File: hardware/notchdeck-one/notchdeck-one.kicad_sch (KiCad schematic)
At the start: 0 parts

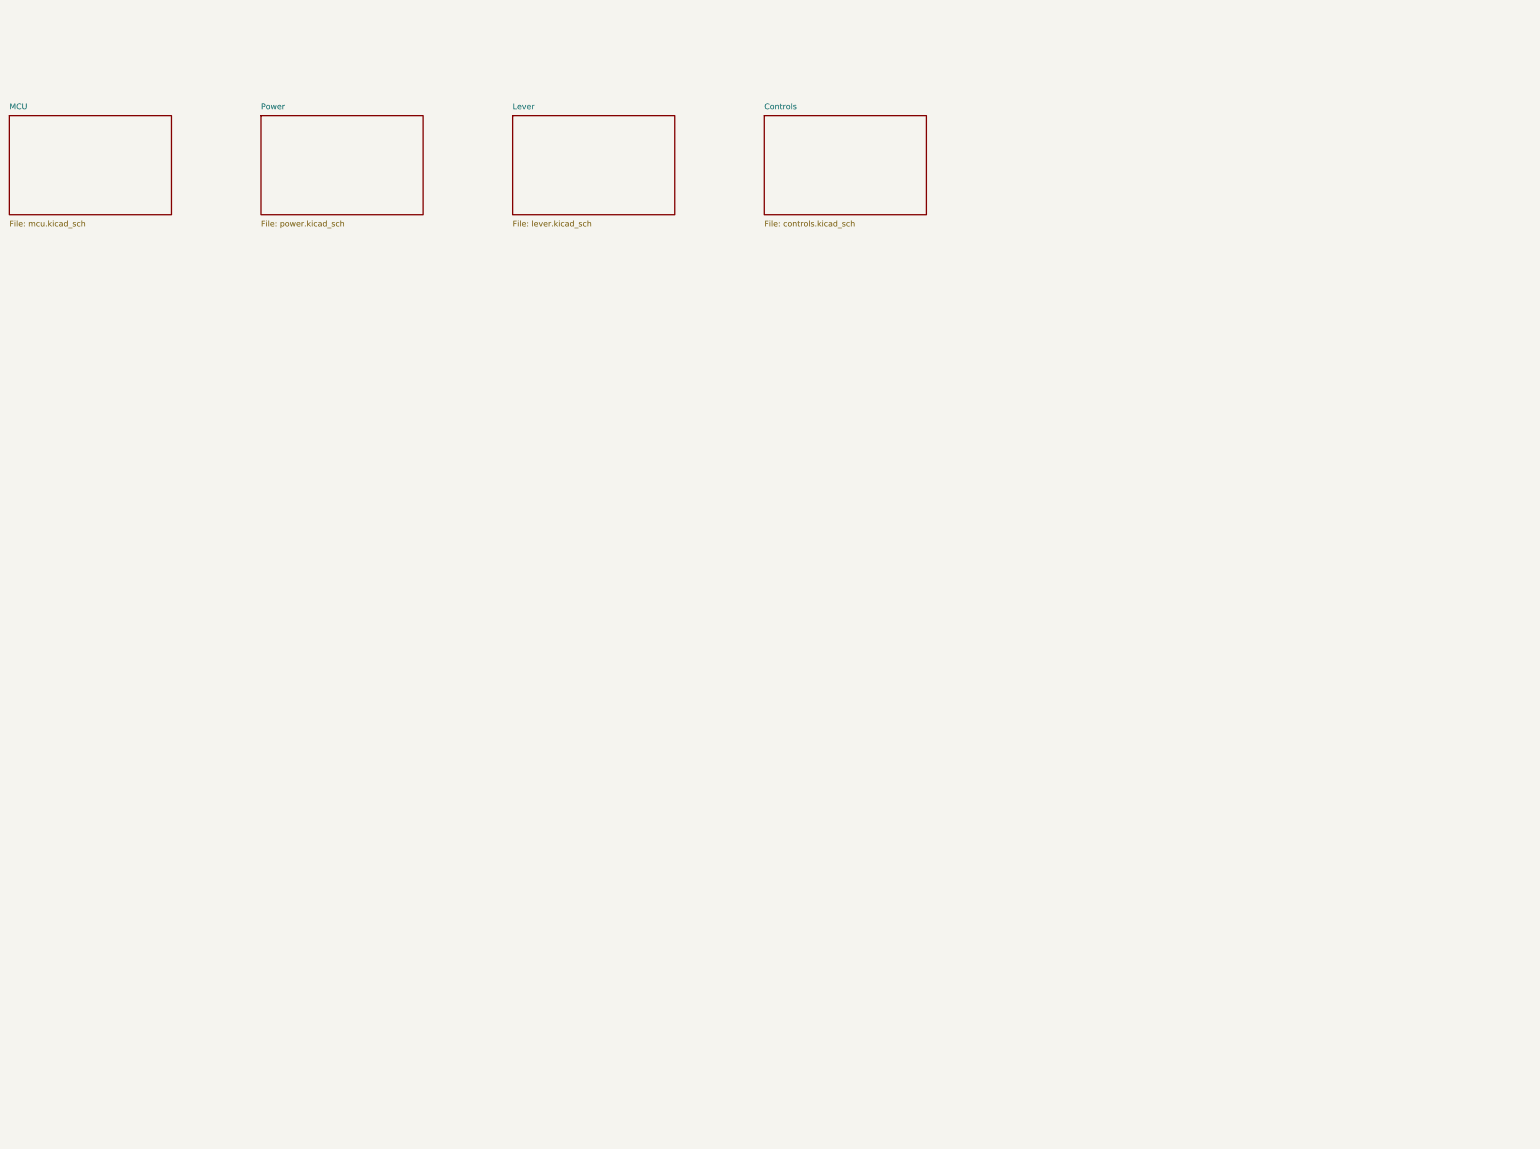
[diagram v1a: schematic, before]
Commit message: Wire and verify NotchDeck controller schematics
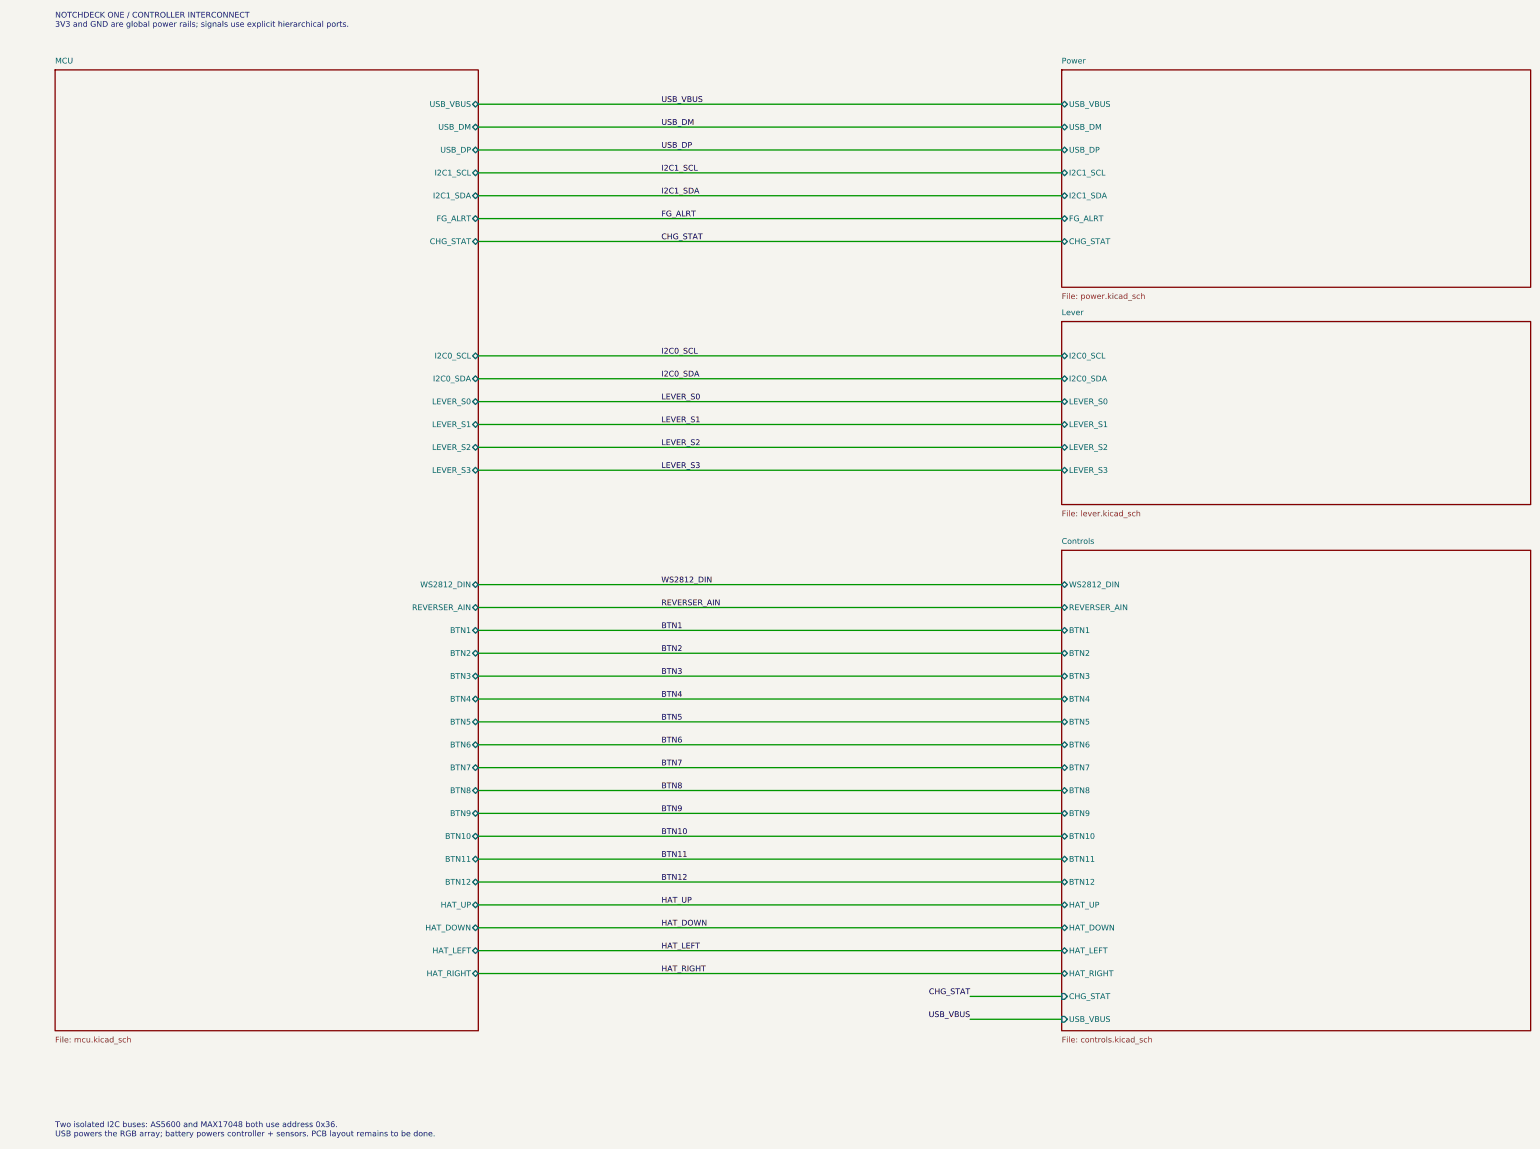
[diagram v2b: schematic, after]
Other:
- sheet Controls ports: added BTN1, BTN10, BTN11, BTN12, BTN2, BTN3, BTN4, BTN5, BTN6, BTN7, BTN8, BTN9, CHG_STAT, HAT_DOWN, HAT_LEFT, HAT_RIGHT, HAT_UP, REVERSER_AIN, USB_VBUS, WS2812_DIN; removed none
- sheet Lever ports: added I2C0_SCL, I2C0_SDA, LEVER_S0, LEVER_S1, LEVER_S2, LEVER_S3; removed none
- sheet MCU ports: added BTN1, BTN10, BTN11, BTN12, BTN2, BTN3, BTN4, BTN5, BTN6, BTN7, BTN8, BTN9, CHG_STAT, FG_ALRT, HAT_DOWN, HAT_LEFT, HAT_RIGHT, HAT_UP, I2C0_SCL, I2C0_SDA, I2C1_SCL, I2C1_SDA, LEVER_S0, LEVER_S1, LEVER_S2, LEVER_S3, REVERSER_AIN, USB_DM, USB_DP, USB_VBUS, WS2812_DIN; removed none
- sheet Power ports: added CHG_STAT, FG_ALRT, I2C1_SCL, I2C1_SDA, USB_DM, USB_DP, USB_VBUS; removed none
- note added: "NOTCHDECK ONE / CONTROLLER INTERCONNECT 3V3 and GND are global power rails; signals use explicit hierarchical ports."
- note added: "Two isolated I2C buses: AS5600 and MAX17048 both use address 0x36. USB powers the RGB array; battery powers controller + sensors. PCB layout remains to be done."

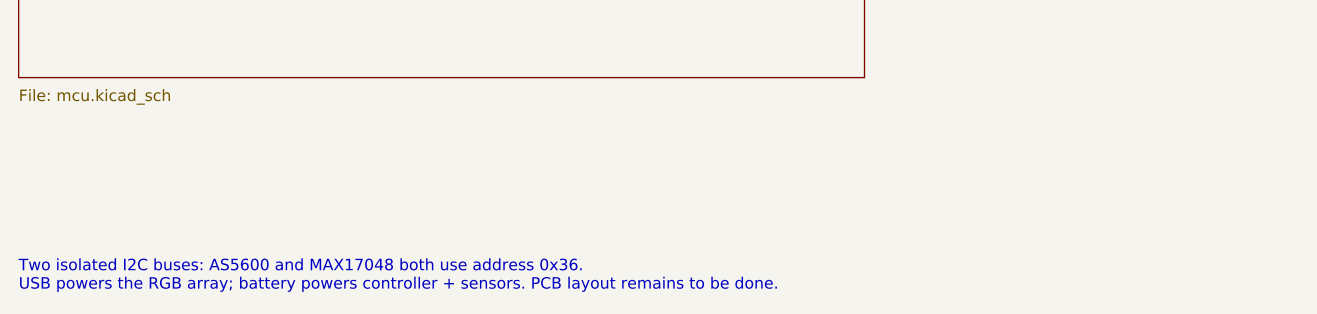
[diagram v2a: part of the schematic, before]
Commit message: Add verified provisional controller PCB floorplan
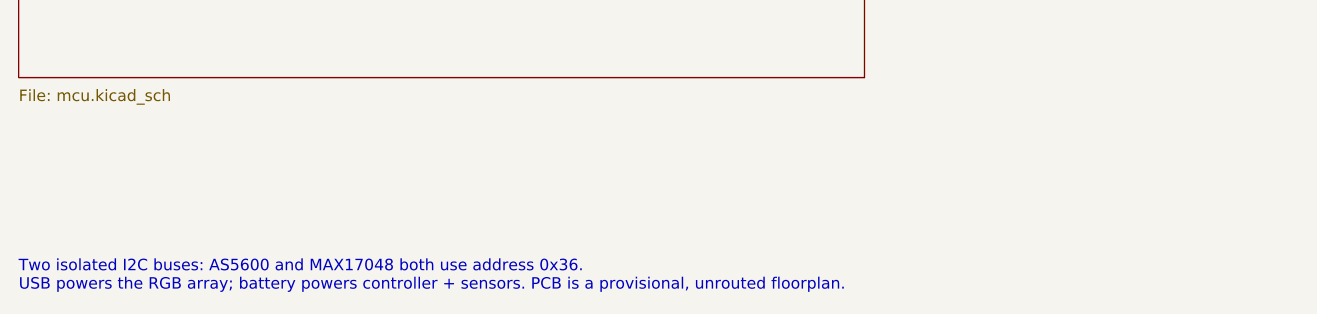
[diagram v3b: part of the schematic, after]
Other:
- note added: "Two isolated I2C buses: AS5600 and MAX17048 both use address 0x36. USB powers the RGB array; battery powers controller + sensors. PCB is a provisional, unrouted floorplan."
- note removed: "Two isolated I2C buses: AS5600 and MAX17048 both use address 0x36. USB powers the RGB array; battery powers controller + sensors. PCB layout remains to be done."
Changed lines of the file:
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@@
 			(effects (font (size 1.27 1.27)) (justify left))
 		)
+		(instances (project "notchdeck-one" (path "/9b1c0f7a-1d2e-4a3b-8c5d-0e6f7a8b9c01" (page "3"))))
 	)
 	(sheet
@@
 			(effects (font (size 1.27 1.27)) (justify left))
 		)
+		(instances (project "notchdeck-one" (path "/9b1c0f7a-1d2e-4a3b-8c5d-0e6f7a8b9c01" (page "4"))))
 	)
 	(sheet
@@
 			(effects (font (size 1.27 1.27)) (justify left))
 		)
+		(instances (project "notchdeck-one" (path "/9b1c0f7a-1d2e-4a3b-8c5d-0e6f7a8b9c01" (page "5"))))
 	)
 	(sheet
@@
 			(effects (font (size 1.27 1.27)) (justify right))
 		)
+		(instances (project "notchdeck-one" (path "/9b1c0f7a-1d2e-4a3b-8c5d-0e6f7a8b9c01" (page "2"))))
 	)
 	(wire (pts (xy 144.7800 38.1000) (xy 274.3200 38.1000))
@@
 		(effects (font (face "Courier New") (size 1.27 1.27)) (justify left top))
 	)
-	(text "Two isolated I2C buses: AS5600 and MAX17048 both use address 0x36.\nUSB powers the RGB array; battery powers controller + sensors. PCB layout remains to be done."
+	(text "Two isolated I2C buses: AS5600 and MAX17048 both use address 0x36.\nUSB powers the RGB array; battery powers controller + sensors. PCB is a provisional, unrouted floorplan."
 		(exclude_from_sim no)
 		(at 50.80 264.16 0)

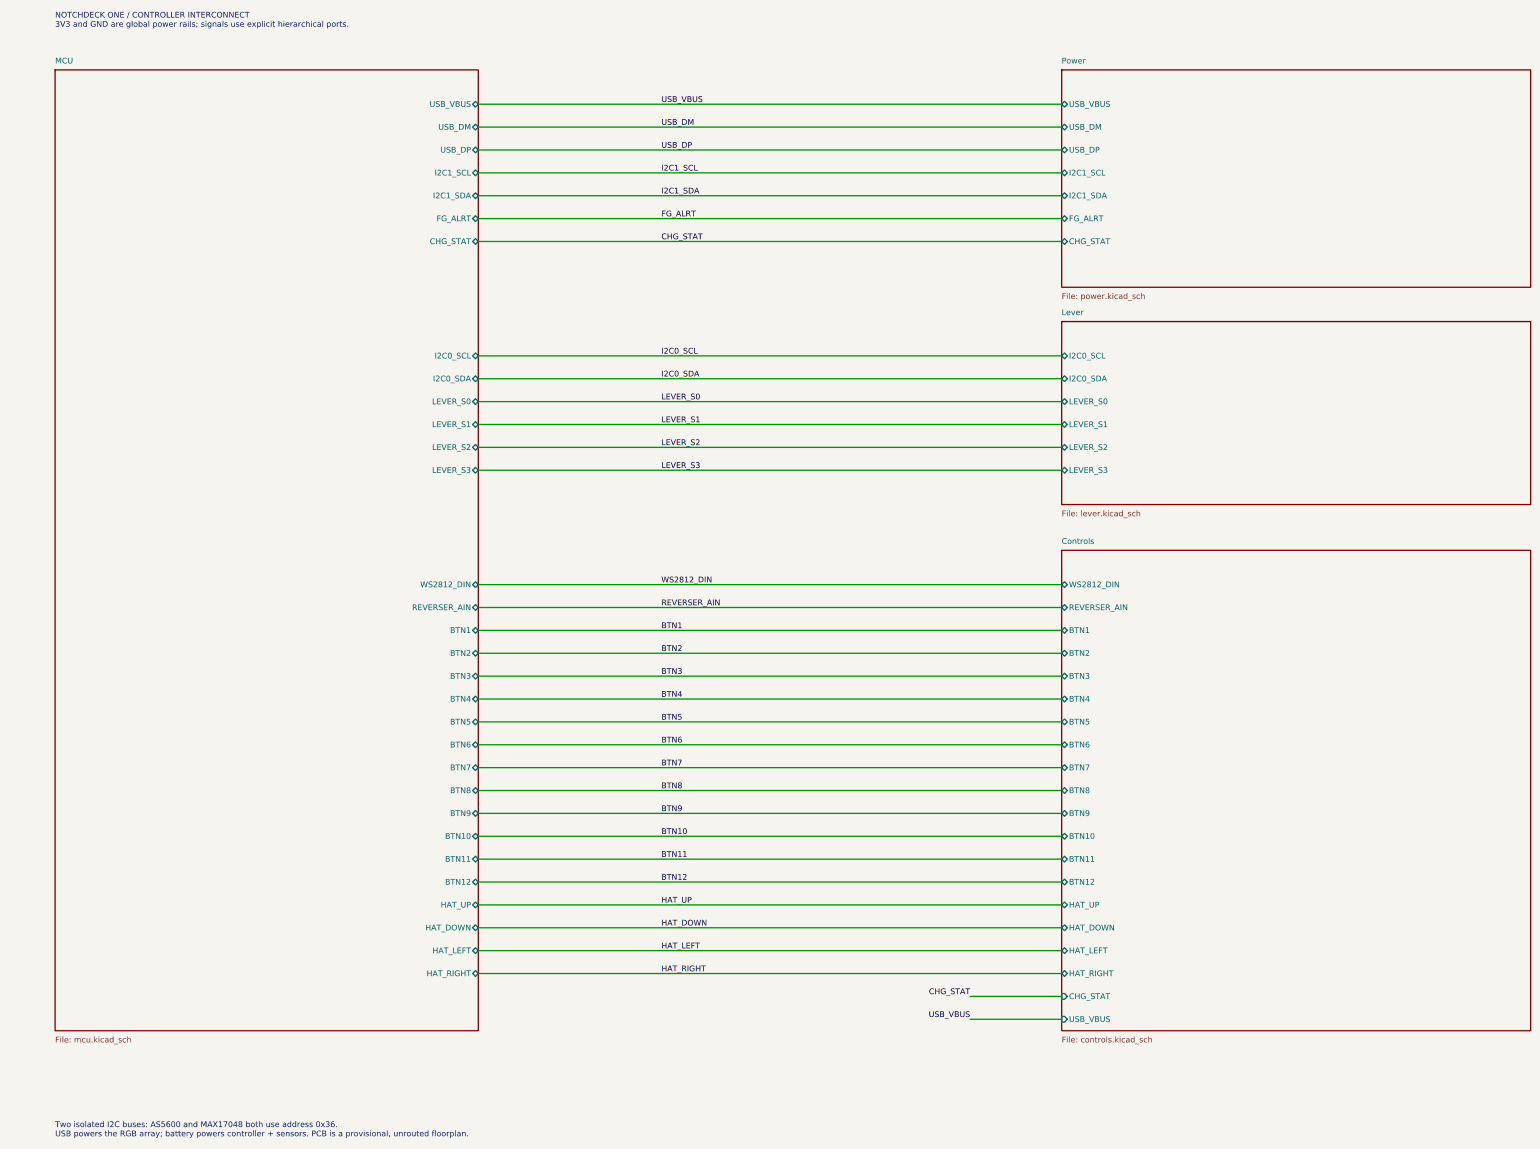
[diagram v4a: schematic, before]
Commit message: Support independent magnetic and Gray-coded power and brake handles
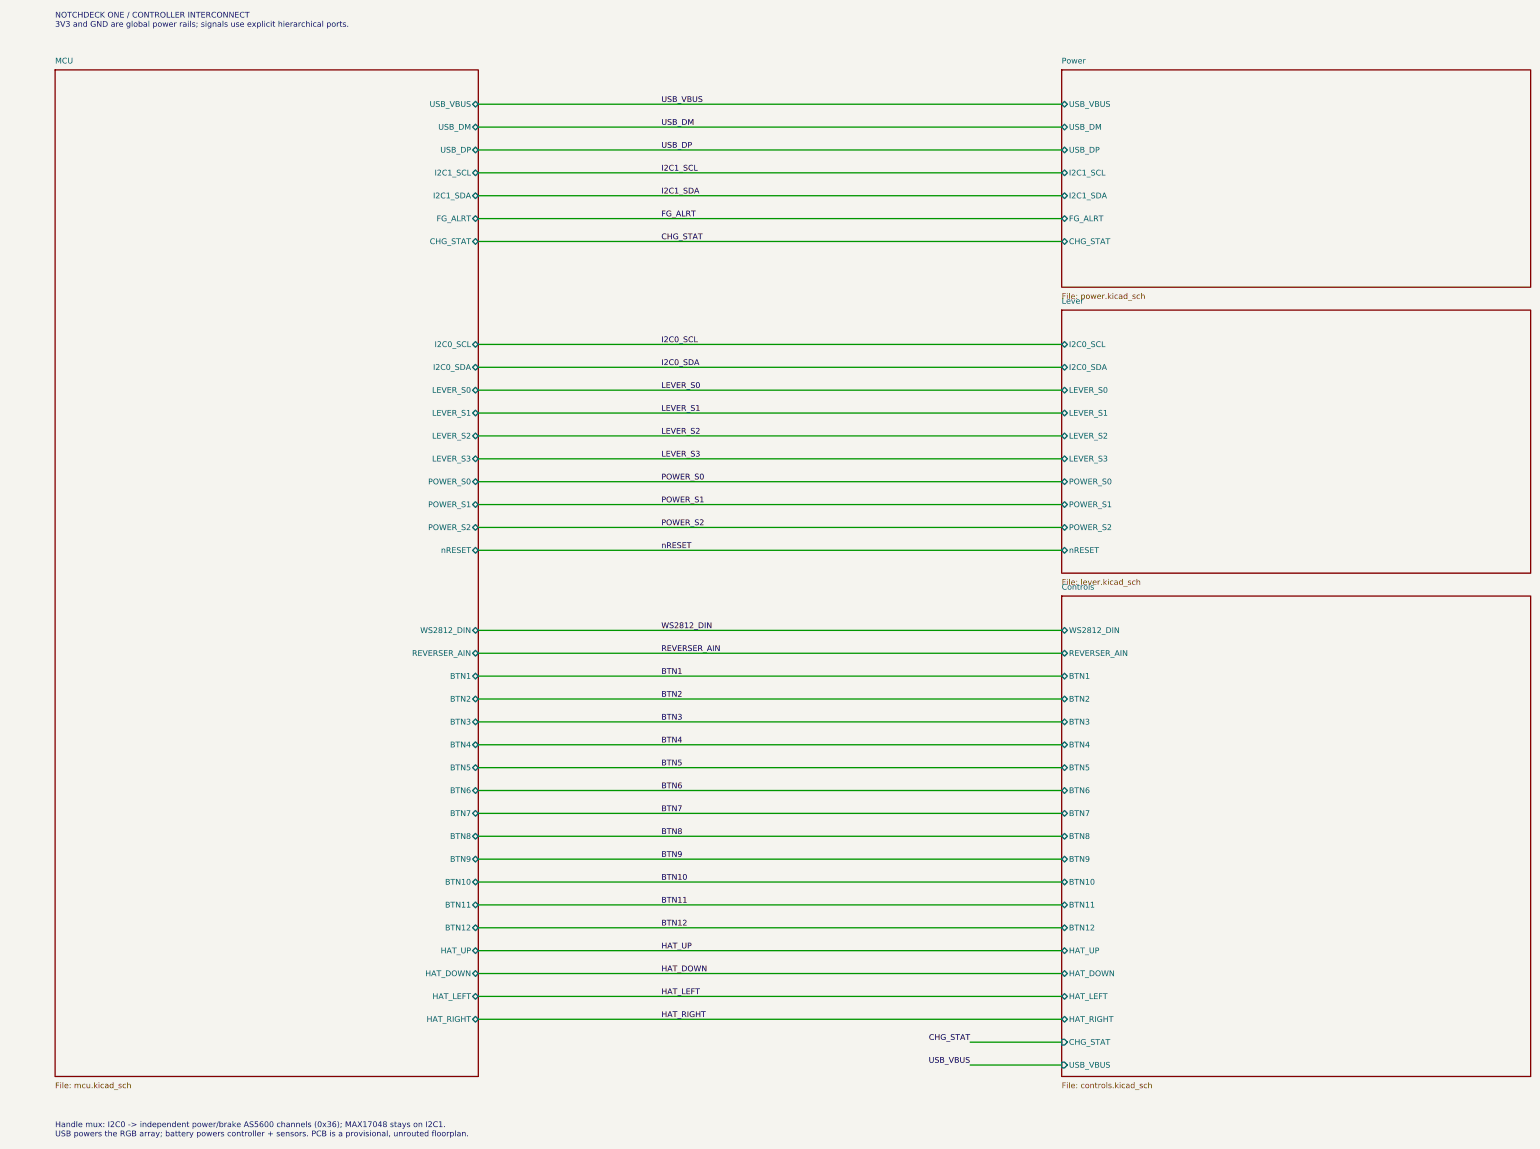
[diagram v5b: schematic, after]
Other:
- sheet Lever ports: added POWER_S0, POWER_S1, POWER_S2, nRESET; removed none
- sheet MCU ports: added POWER_S0, POWER_S1, POWER_S2, nRESET; removed none
- note added: "Handle mux: I2C0 -> independent power/brake AS5600 channels (0x36); MAX17048 stays on I2C1. USB powers the RGB array; battery powers controller + sensors. PCB is a provisional, unrouted floorplan."
- note removed: "Two isolated I2C buses: AS5600 and MAX17048 both use address 0x36. USB powers the RGB array; battery powers controller + sensors. PCB is a provisional, unrouted floorplan."
